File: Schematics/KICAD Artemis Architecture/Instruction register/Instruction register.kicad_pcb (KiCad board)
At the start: 4 copper layers, 82.7 x 41.5 mm, 44 parts, among them J1 Power, J2 Control, J3 BUS LB, J4 BUS UB, J5 Instruction Out, U1 74LS173, U2 74LS245, U3 74LS173, U4 74LS173, U5 74LS173, U6 74LS245

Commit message: Instruction Register Complete
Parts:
- added C2: 0.1 uF, Capacitor_SMD:C_1206_3216Metric_Pad1.33x1.80mm_HandSolder, F.Cu at (152.8, 45.4)
- moved C1 1.00 mm to (152.8, 48.0)
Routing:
- net /CLR: track 116.4 -> 124.2 mm
- net GNDREF: track 227.9 -> 231.0 mm
- net VCC: track 243.2 -> 242.2 mm
- net /~{DO}: track 75.3 -> 74.5 mm
- net Net-(D9-A): track 53.6 -> 53.0 mm
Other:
- board text added: "74LS173"
- board text added: "74LS245"
- board text added: "BUS LB"
- board text added: "BUS UB"
- board text added: "Control"
- board text added: "D"
- board text added: "George Sleen V1"
- board text added: "Instruction Out"
- board text added: "Operand"
- board text added: "Operation"
- board text added: "Power"
- board text added: "R"

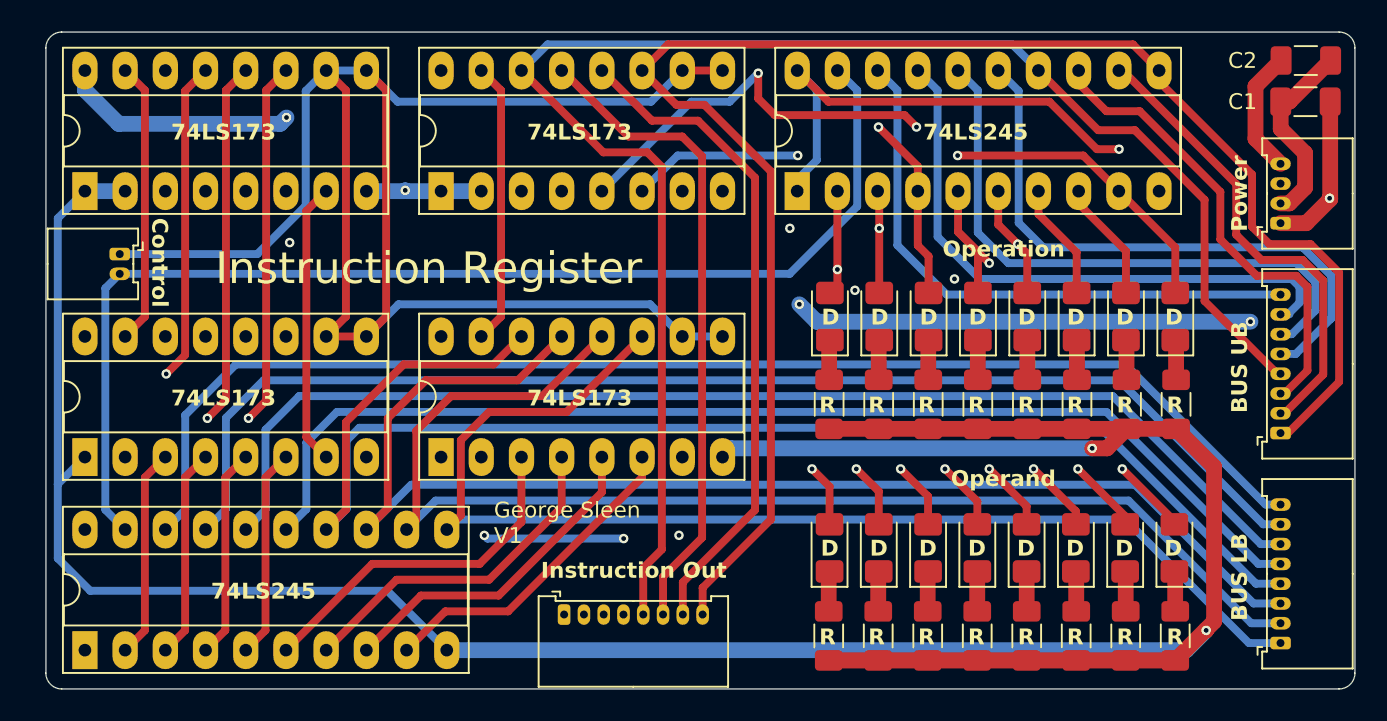
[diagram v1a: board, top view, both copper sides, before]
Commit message: Added Decoupling Caps
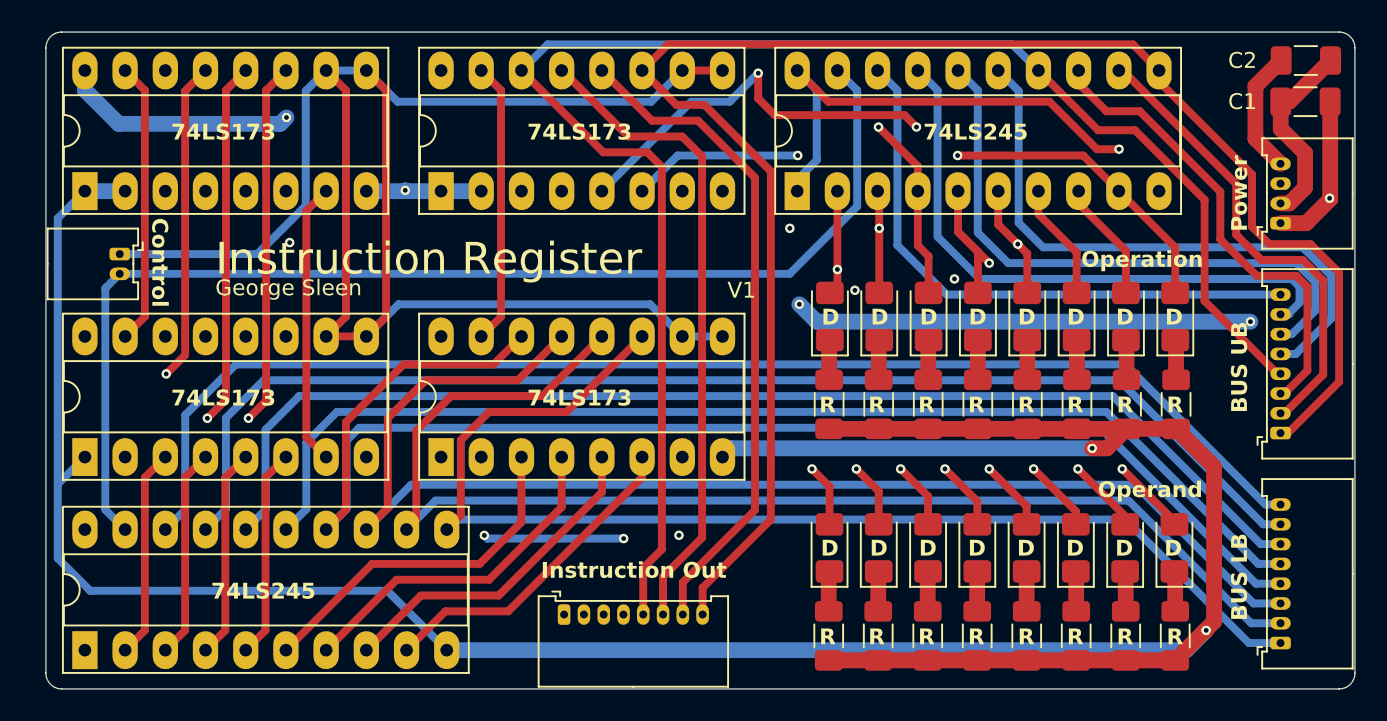
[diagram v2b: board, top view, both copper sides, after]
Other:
- board text added: "George Sleen"
- board text added: "V1"
- board text removed: "George Sleen V1"
